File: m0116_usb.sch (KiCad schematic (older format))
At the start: 180 parts, among them J1 AVR-ISP-6, J2 Conn_01x04, J3 Conn_01x04, U1 ATmega32A-PU, Y1 Resonator

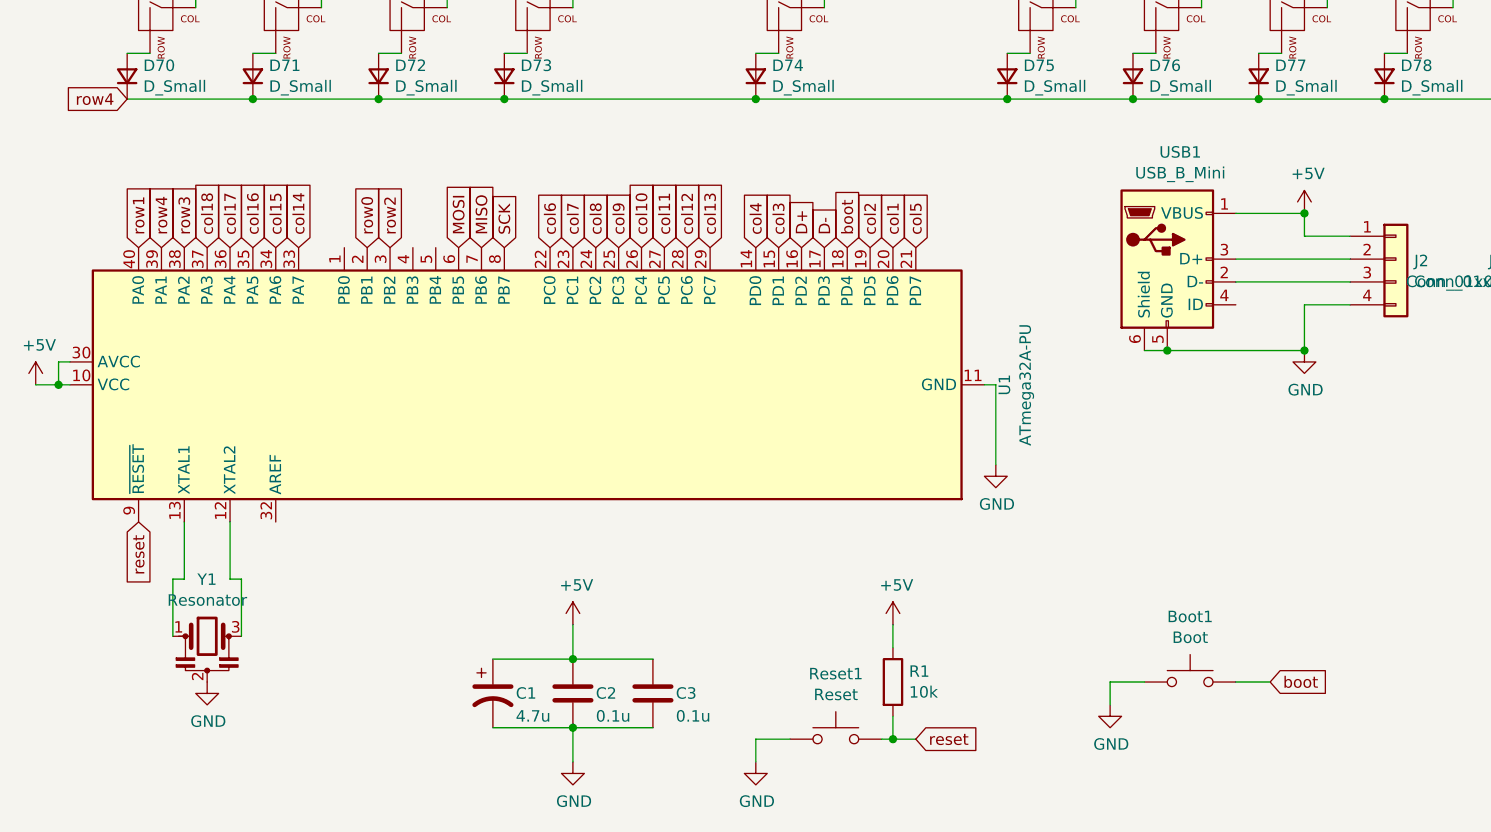
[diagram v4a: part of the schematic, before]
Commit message: change JST connector size
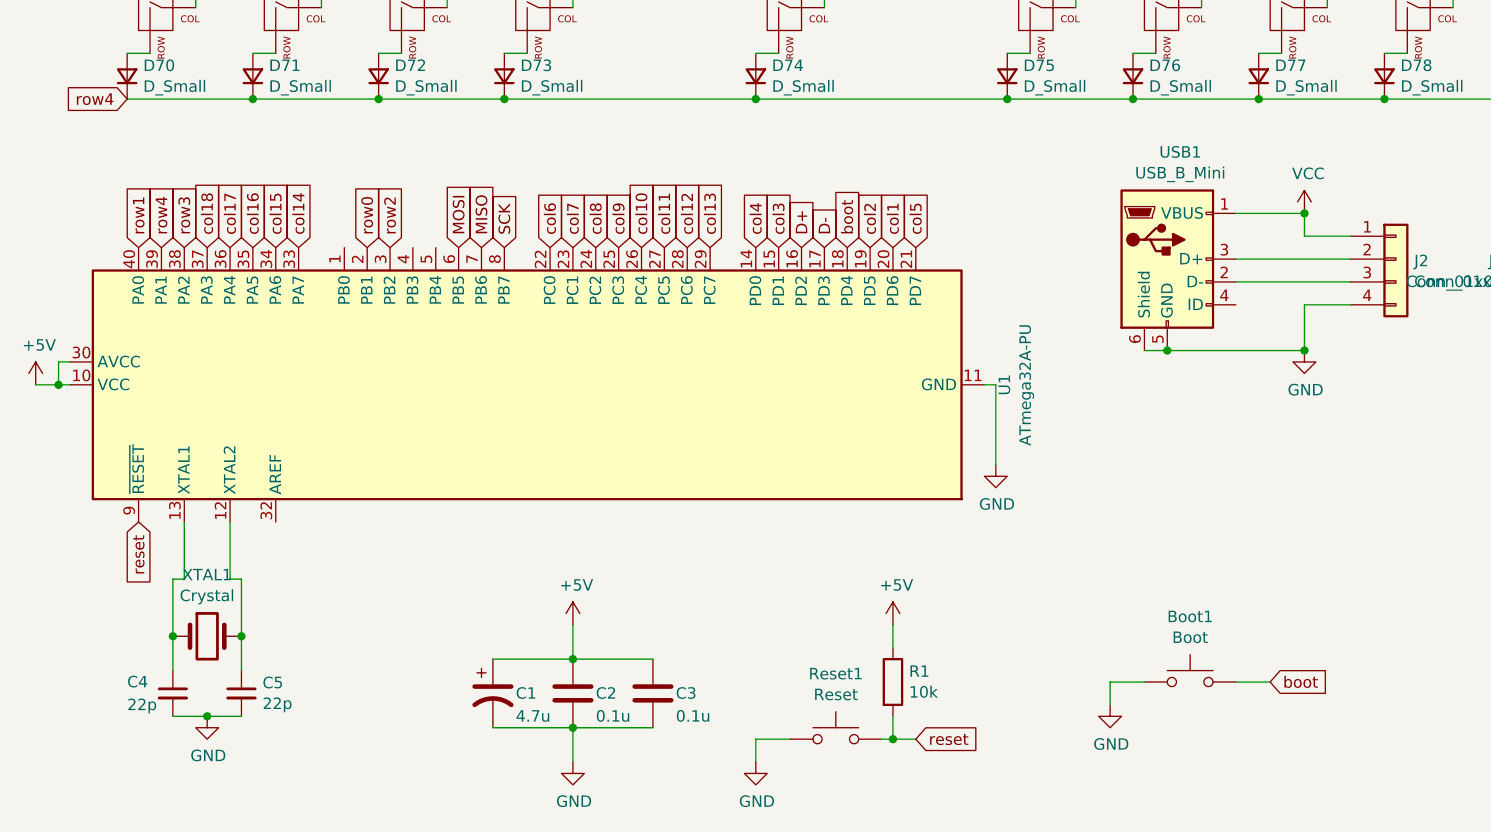
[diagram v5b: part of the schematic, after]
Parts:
- removed Y1: Resonator, Crystal:Resonator-3Pin_W7.0mm_H2.5mm, symbol Device:Resonator
- added C4, C5: 22p, Capacitor_THT:C_Disc_D6.0mm_W2.5mm_P5.00mm, symbol Device:C_Small
- added XTAL1: Crystal, Crystal:Crystal_HC49-4H_Vertical, symbol Device:Crystal
- J3: footprint Connector_JST:JST_EH_B4B-EH-A_1x04_P2.50mm_Vertical -> Connector_JST:JST_PH_S4B-PH-K_1x04_P2.00mm_Horizontal
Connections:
- net +5V: no longer J2.1 (Pin_1), USB1.1 (VBUS)
- net GND: now also C4.2, C5.2
- net VCC: now also J2.1 (Pin_1), USB1.1 (VBUS)
- net at U1.12 (XTAL2): now also C5.1, XTAL1.2
- net at U1.13 (XTAL1): now also C4.1, XTAL1.1
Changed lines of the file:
@@
 L power:GND #PWR014
 U 1 1 5EC20D0B
-P 1450 6850
-F 0 "#PWR014" H 1450 6600 50  0001 C CNN
-F 1 "GND" H 1455 6677 50  0000 C CNN
-F 2 "" H 1450 6850 50  0001 C CNN
-F 3 "" H 1450 6850 50  0001 C CNN
-	1    1450 6850
+P 1450 7000
+F 0 "#PWR014" H 1450 6750 50  0001 C CNN
+F 1 "GND" H 1455 6827 50  0000 C CNN
+F 2 "" H 1450 7000 50  0001 C CNN
+F 3 "" H 1450 7000 50  0001 C CNN
+	1    1450 7000
 	1    0    0    -1
 $EndComp
@@
 L power:VCC #PWR02
 U 1 1 5EC6654A
-P 7450 4900
-F 0 "#PWR02" H 7450 4750 50  0001 C CNN
-F 1 "VCC" H 7467 5073 50  0000 C CNN
-F 2 "" H 7450 4900 50  0001 C CNN
-F 3 "" H 7450 4900 50  0001 C CNN
-	1    7450 4900
+P 6250 4800
+F 0 "#PWR02" H 6250 4650 50  0001 C CNN
+F 1 "VCC" H 6267 4973 50  0000 C CNN
+F 2 "" H 6250 4800 50  0001 C CNN
+F 3 "" H 6250 4800 50  0001 C CNN
+	1    6250 4800
 	1    0    0    -1
 $EndComp
@@
 F 0 "J3" H 7280 4992 50  0000 L CNN
 F 1 "Conn_01x04" H 7280 4901 50  0000 L CNN
-F 2 "Connector_JST:JST_EH_B4B-EH-A_1x04_P2.50mm_Vertical" H 7200 5000 50  0001 C CNN
+F 2 "Connector_JST:JST_PH_S4B-PH-K_1x04_P2.00mm_Horizontal" H 7200 5000 50  0001 C CNN
 F 3 "~" H 7200 5000 50  0001 C CNN
 	1    7200 5000
@@
 Wire Wire Line
 	5550 5400 5650 5400
-$Comp
-L Device:Resonator Y1
-U 1 1 5EE0DEF7
-P 1450 6650
-F 0 "Y1" H 1450 6898 50  0000 C CNN
-F 1 "Resonator" H 1450 6807 50  0000 C CNN
-F 2 "Crystal:Resonator-3Pin_W7.0mm_H2.5mm" H 1425 6650 50  0001 C CNN
-F 3 "~" H 1425 6650 50  0001 C CNN
-	1    1450 6650
-	1    0    0    -1
-$EndComp
 Wire Wire Line
 	1300 6400 1300 6650
@@
 	7550 5200 7400 5200
 Wire Wire Line
-	7400 4900 7450 4900
-Wire Wire Line
 	5950 4800 6250 4800
-Connection ~ 7450 4900
-Wire Wire Line
-	7450 4900 7550 4900
-$Comp
-L power:GND #PWR?
+$Comp
+L power:GND #PWR0101
 U 1 1 5EFE9A5B
 P 6250 5400
-F 0 "#PWR?" H 6250 5150 50  0001 C CNN
+F 0 "#PWR0101" H 6250 5150 50  0001 C CNN
 F 1 "GND" H 6255 5227 50  0000 C CNN
 F 2 "" H 6250 5400 50  0001 C CNN
@@
 Connection ~ 6250 5400
 $Comp
-L power:+5V #PWR?
-U 1 1 5EFEA06A
-P 6250 4800
-F 0 "#PWR?" H 6250 4650 50  0001 C CNN
-F 1 "+5V" H 6265 4973 50  0000 C CNN
-F 2 "" H 6250 4800 50  0001 C CNN
-F 3 "" H 6250 4800 50  0001 C CNN
-	1    6250 4800
-	1    0    0    -1
-$EndComp
+L Device:Crystal XTAL1
+U 1 1 5F006AA5
+P 1450 6650
+F 0 "XTAL1" H 1450 6918 50  0000 C CNN
+F 1 "Crystal" H 1450 6827 50  0000 C CNN
+F 2 "Crystal:Crystal_HC49-4H_Vertical" H 1450 6650 50  0001 C CNN
+F 3 "~" H 1450 6650 50  0001 C CNN
+	1    1450 6650
+	1    0    0    -1
+$EndComp
+$Comp
+L Device:C_Small C4
+U 1 1 5F007CAF
+P 1300 6900
+F 0 "C4" H 1100 6950 50  0000 L CNN
+F 1 "22p" H 1100 6850 50  0000 L CNN
+F 2 "Capacitor_THT:C_Disc_D6.0mm_W2.5mm_P5.00mm" H 1300 6900 50  0001 C CNN
+F 3 "~" H 1300 6900 50  0001 C CNN
+	1    1300 6900
+	1    0    0    -1
+$EndComp
+$Comp
+L Device:C_Small C5
+U 1 1 5F009381
+P 1600 6900
+F 0 "C5" H 1692 6946 50  0000 L CNN
+F 1 "22p" H 1692 6855 50  0000 L CNN
+F 2 "Capacitor_THT:C_Disc_D6.0mm_W2.5mm_P5.00mm" H 1600 6900 50  0001 C CNN
+F 3 "~" H 1600 6900 50  0001 C CNN
+	1    1600 6900
+	1    0    0    -1
+$EndComp
+Wire Wire Line
+	1300 6650 1300 6800
+Connection ~ 1300 6650
+Wire Wire Line
+	1600 6650 1600 6800
+Connection ~ 1600 6650
+Wire Wire Line
+	1300 7000 1450 7000
+Connection ~ 1450 7000
+Wire Wire Line
+	1450 7000 1600 7000
 Connection ~ 6250 4800
+Wire Wire Line
+	7400 4900 7450 4900
+$Comp
+L power:VCC #PWR0102
+U 1 1 5EE56FF8
+P 7450 4900
+F 0 "#PWR0102" H 7450 4750 50  0001 C CNN
+F 1 "VCC" H 7467 5073 50  0000 C CNN
+F 2 "" H 7450 4900 50  0001 C CNN
+F 3 "" H 7450 4900 50  0001 C CNN
+	1    7450 4900
+	1    0    0    -1
+$EndComp
+Connection ~ 7450 4900
+Wire Wire Line
+	7450 4900 7550 4900
 $EndSCHEMATC

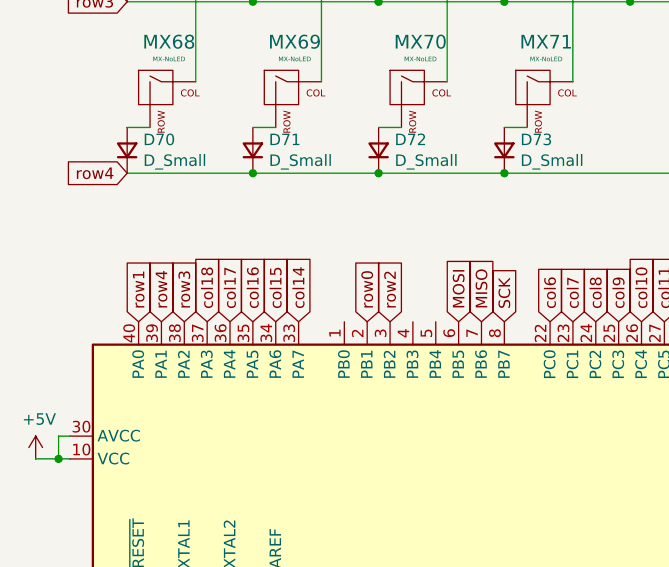
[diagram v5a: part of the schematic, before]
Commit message: fixed clearance issues with buttons
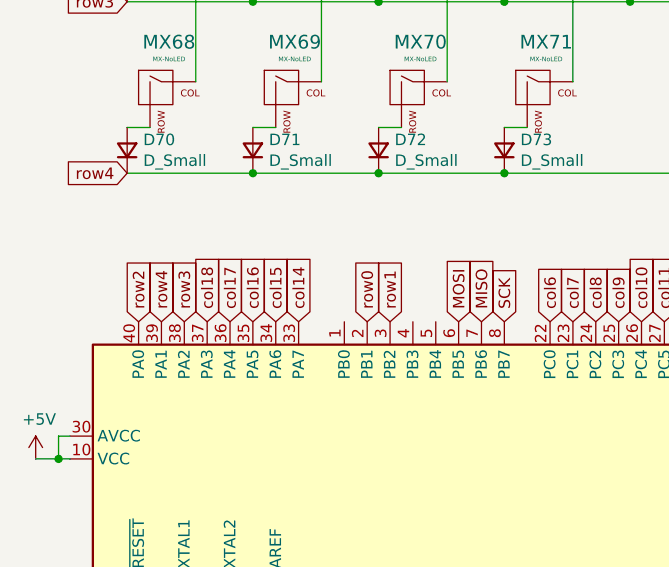
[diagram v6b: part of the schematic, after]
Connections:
- net row1: now also U1.3 (PB2); no longer U1.40 (PA0)
- net row2: now also U1.40 (PA0); no longer U1.3 (PB2)
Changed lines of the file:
@@
 Text GLabel 2150 4950 1    50   Input ~ 0
 row0
+Text GLabel 2250 4950 1    50   Input ~ 0
+row1
 Text GLabel 1150 4950 1    50   Input ~ 0
-row1
-Text GLabel 2250 4950 1    50   Input ~ 0
 row2
 Text GLabel 1350 4950 1    50   Input ~ 0
